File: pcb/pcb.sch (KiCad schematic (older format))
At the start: 96 parts, among them J1 USB_C_Receptacle_USB2.0, Q1 DTC123J, SW1 SW_Push, SW10 SW_PUSH, SW11 SW_PUSH, SW12 SW_PUSH, SW13 SW_PUSH, SW14 SW_PUSH, SW15 SW_PUSH, SW16 SW_PUSH, SW17 SW_PUSH, SW18 SW_PUSH, SW19 SW_PUSH, SW2 SW_PUSH, SW20 SW_PUSH, SW21 SW_PUSH, SW22 SW_PUSH, SW23 SW_PUSH, SW24 SW_PUSH, SW25 SW_PUSH, SW26 SW_PUSH, SW27 SW_PUSH, SW28 SW_PUSH, SW29 SW_PUSH, SW3 SW_PUSH, SW30 SW_PUSH, SW31 SW_PUSH, SW32 SW_PUSH, SW33 SW_PUSH, SW34 Rotary_Encoder_Switch, SW4 SW_PUSH, SW5 SW_PUSH, SW6 SW_PUSH, SW7 SW_PUSH, SW8 SW_PUSH, SW9 SW_PUSH, U1 STM32F072CBTx, U2 MCP1700-3002E_SOT23, U3 SRV05-4

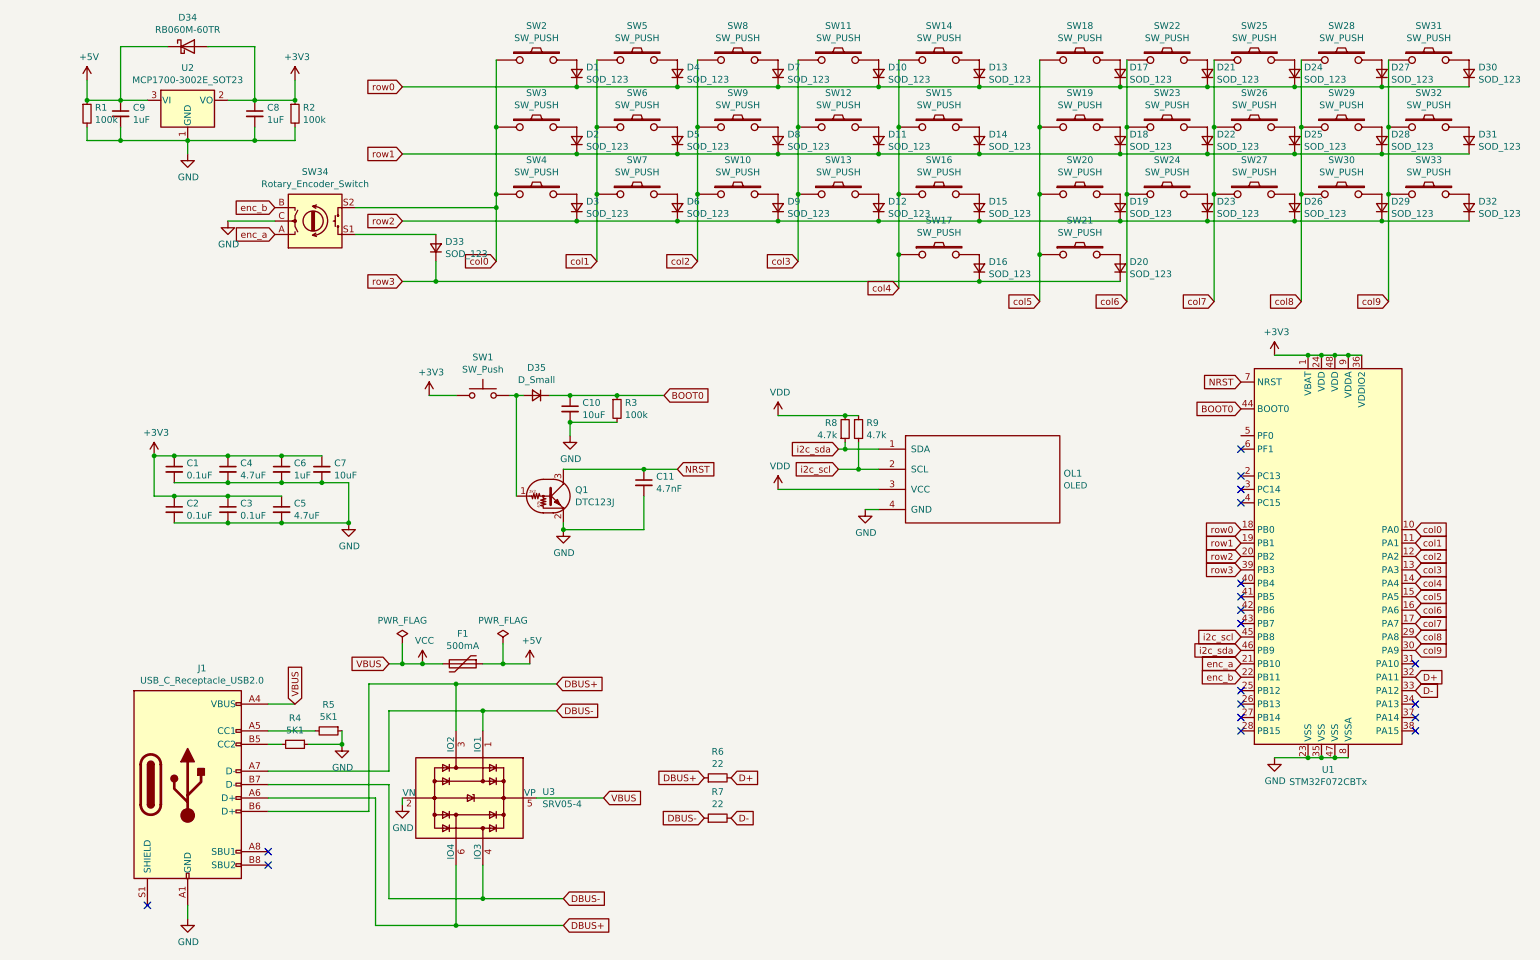
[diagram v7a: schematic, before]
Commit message: Finishes transition to arm / usb c
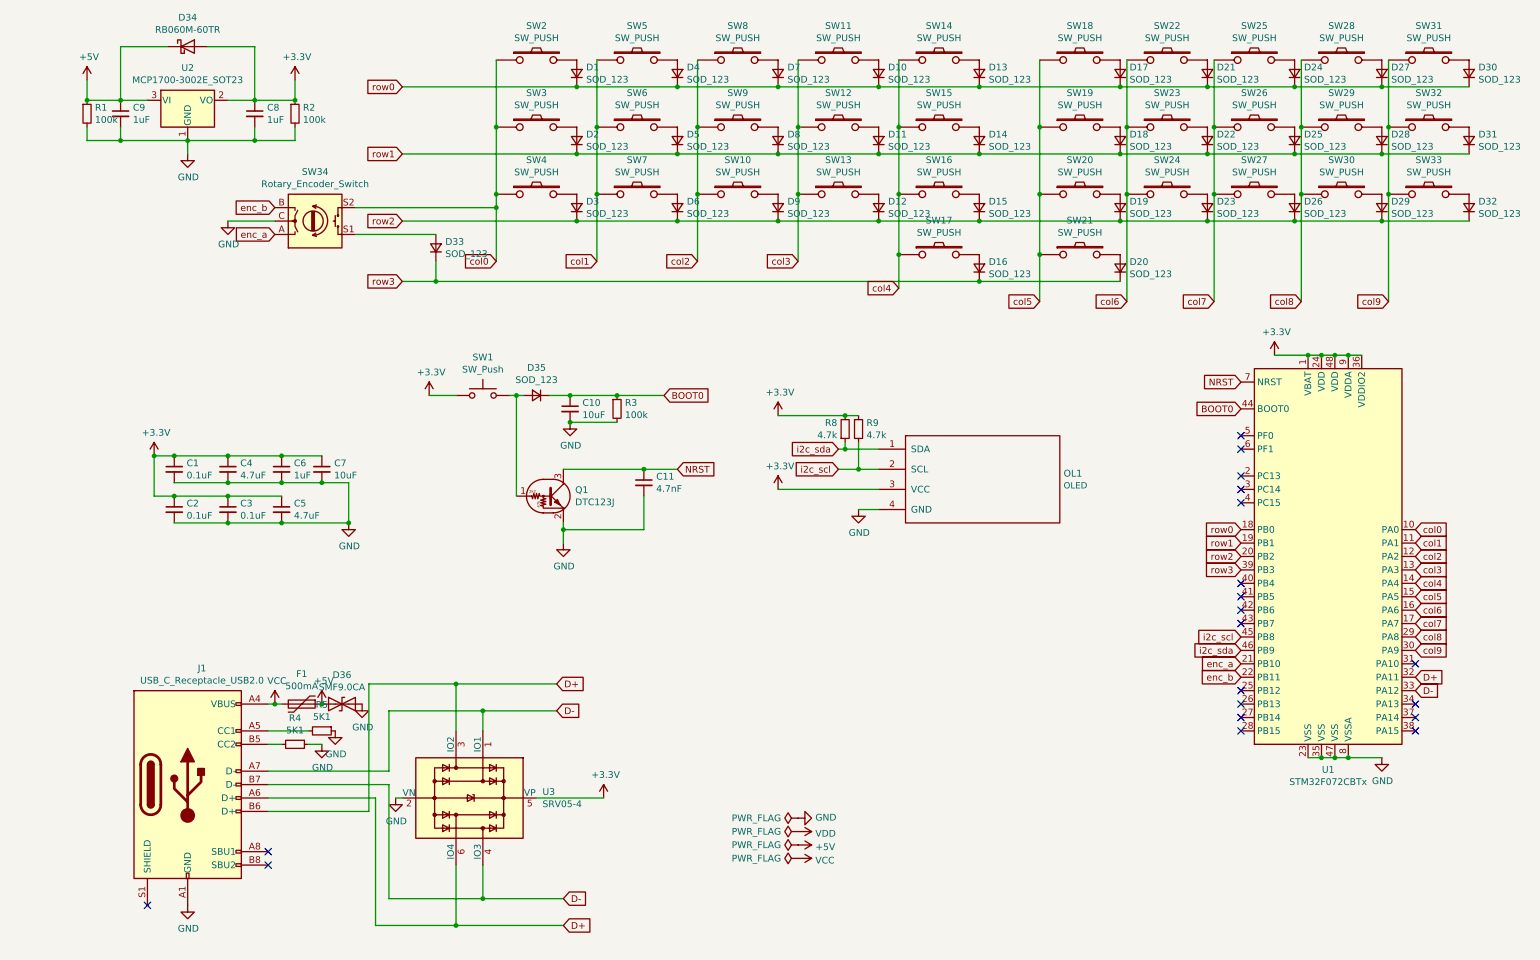
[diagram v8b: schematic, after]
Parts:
- removed R6, R7: 22, Resistor_SMD:R_0805_2012Metric, symbol Device:R_Small
- added D36: SMF9.0CA, Diode_SMD:D_SOD-123, symbol Device:D_TVS
- D35: value D_Small -> SOD_123
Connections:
- net DBUS+ is gone; now on net D+: J1.A6 (D+), J1.B6 (D+), U3.3 (IO2), U3.6 (IO4)
- net DBUS- is gone; now on net D-: J1.A7 (D-), J1.B7 (D-), U3.1 (IO1), U3.4 (IO3)
- net +3V3: now also OL1.3 (VCC), R8.2, R9.1, U3.5 (VP)
- net +5V: now also D36.1 (A1)
- net GND: now also D36.2 (A2)
- net VCC: no longer U3.5 (VP)
- net VDD: no longer OL1.3 (VCC), R8.2, R9.1
- no-connect marks 19 -> 20
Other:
- moved on the sheet: F1, R5
